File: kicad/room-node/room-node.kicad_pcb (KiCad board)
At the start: 4 copper layers, 90 x 50 mm, 59 parts, among them J1 USB4085-GF-A, J2 Speaker 8Ω, J3 Waveshare e-paper, J4 LED strip, SW1 TL3342 RESET, SW2 TL3342 BOOT, SW3 TL3342 VOICE, U1 ESP32-S3-WROOM-1-N16R8, U2 AP7361C-33ER-13, U3 MAX98357AETE+, U5 USBLC6-2SC6, U6 AHT20

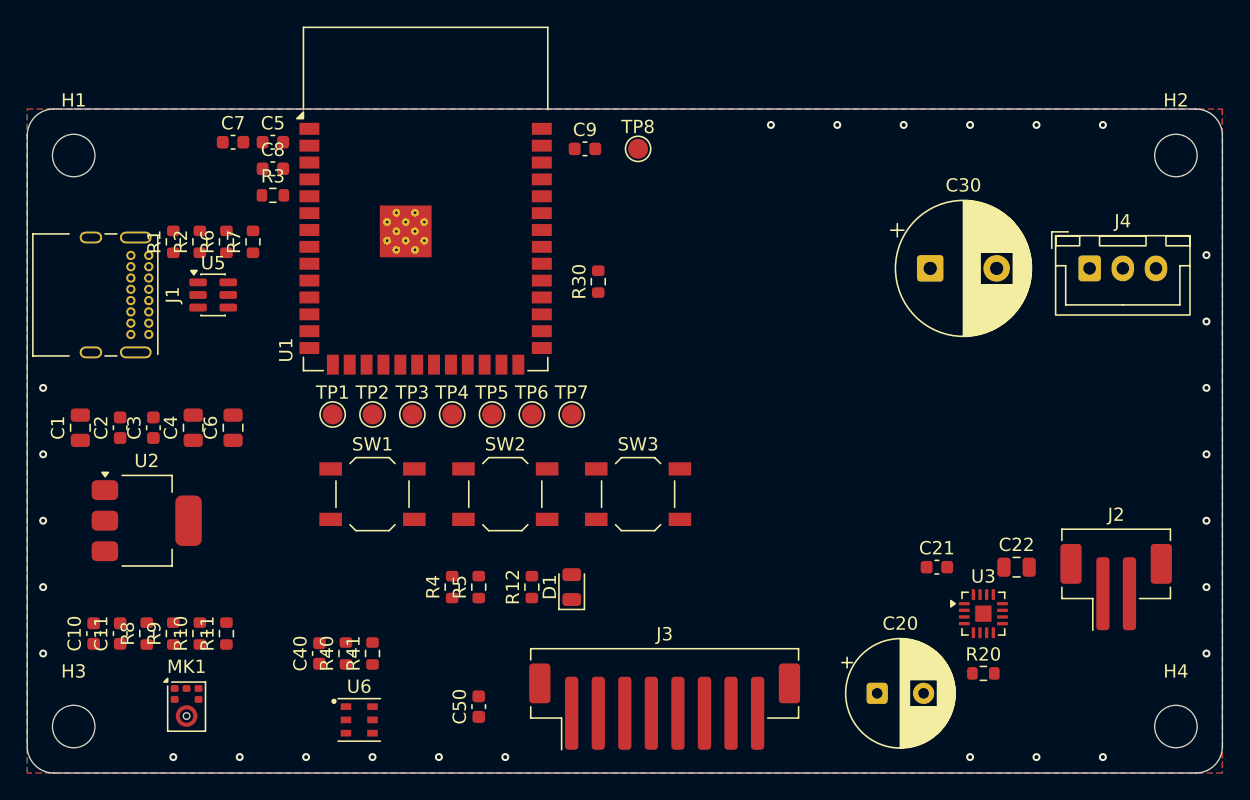
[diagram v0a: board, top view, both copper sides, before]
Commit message: SQU-17: full rev A board — display-size outline, placement and routing
Board matches the Waveshare 2.9" e-paper module (89.5 x 38 mm, 4 x M2 on its
84.5 x 33 mm hole pattern) so it screws behind the display on standoffs.
All 55 parts placed and every net routed (Freerouting + hand routes for J1 VBUS,
amp pins and the AHT20 island). L2 GND, L3 +3V3 planes; +5V as a 0.6-1.0 mm
track. DRC: 0 errors, 0 unconnected, 0 parity issues; 53 silkscreen warnings.

tools/pcb_build.py replaces tools/pcb_setup.py. Gerbers in reports/fab/.

Co-Authored-By: Claude Opus 5.5 <noreply@anthropic.com>
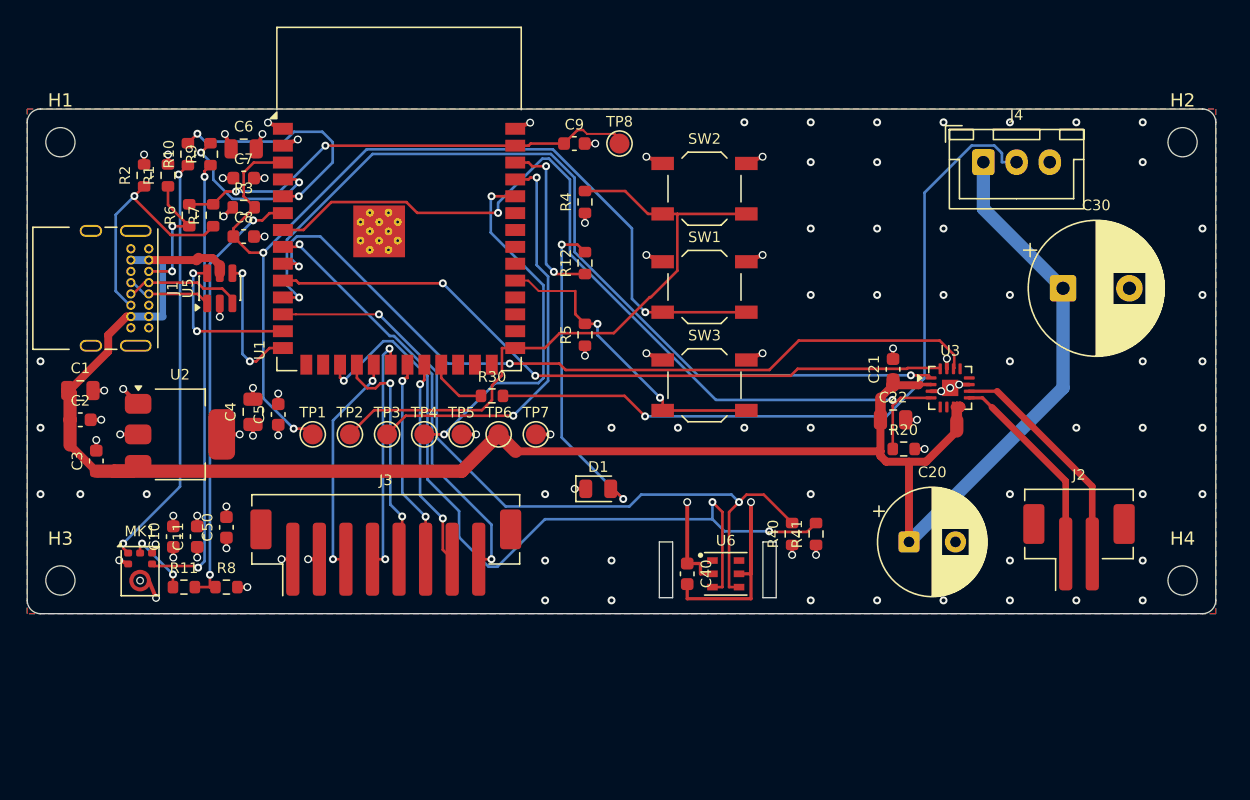
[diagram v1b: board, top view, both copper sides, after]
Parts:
- H1, H2, H3, H4: value M3 -> M2; footprint MountingHole:MountingHole_3.2mm_M3 -> MountingHole:MountingHole_2.2mm_M2
- moved R9 36.2 mm to (113.8, 103.4)
- moved R10 36.1 mm to (112.1, 103.4)
- moved R40 34.8 mm to (157.6, 132.0)
- moved R41 34.6 mm to (159.4, 132.0)
- moved R4 30.7 mm to (142.0, 107.0)
- moved U6 29.7 mm to (152.6, 135.0)
- moved SW1 29.5 mm to (151.0, 113.4)
- moved C40 28.3 mm to (149.7, 135.0), turned to -90 degrees
- moved SW2 27.5 mm to (151.0, 106.0)
- moved R12 24.7 mm to (142.0, 111.6)
- moved J3 24.0 mm to (127.0, 133.4)
- moved C50 23.3 mm to (115.0, 131.5)
- moved C6 21.0 mm to (116.3, 103.0), turned to 0 degrees
- moved R5 20.6 mm to (142.0, 117.0)
- moved C5 20.5 mm to (118.9, 123.0), turned to 90 degrees
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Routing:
- net +5V: track 0.00 -> 154.3 mm
- net EN: track 0.00 -> 75.4 mm, vias 0 -> 3
- net I2S_SPK_DIN: track 0.00 -> 67.4 mm, vias 0 -> 2
- net AMP_SD: track 0.00 -> 66.8 mm, vias 0 -> 2
- net I2C_SCL: track 0.00 -> 61.8 mm, vias 0 -> 3
- net I2S_SPK_LRCLK: track 0.00 -> 60.1 mm, vias 0 -> 2
- net Net-(J4-Pin_2): track 0.00 -> 56.9 mm, vias 0 -> 1
- net I2C_SDA: track 0.00 -> 56.4 mm, vias 0 -> 2
- net I2S_SPK_BCLK: track 0.00 -> 52.7 mm, vias 0 -> 2
- net GND: track 0.00 -> 49.7 mm, vias 27 -> 89
- net IO0: track 0.00 -> 48.8 mm
- net CC_SENSE: track 0.00 -> 35.3 mm, vias 0 -> 2
- net Net-(MK1-BCLK): track 0.00 -> 34.3 mm, vias 0 -> 2
- net I2S_MIC_DATA: track 0.00 -> 33.0 mm, vias 0 -> 2
- net EPD_BUSY: track 0.00 -> 32.2 mm, vias 0 -> 2
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- removed copper zone on In2.Cu, net +5V
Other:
- board size 90 x 50 mm -> 89.5 x 38 mm

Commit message: SQU-17: remove voice button SW3 + R5 (wake word only)
Chris: no voice button. U1 pin 31 (GPIO38) gets a no-connect flag.
Schematic, board (parts, 13 tracks/vias, +3V3 stub), BOM, docs,
pinout check and pcb_build.py updated. Gerbers, PDF, pictures regenerated.
ERC: 0 errors, 1 accepted warning. DRC: 0 errors, 0 unconnected,
0 parity issues, 53 silkscreen warnings. Pinout check: PASS.

Co-Authored-By: Claude Opus 5.5 <noreply@anthropic.com>
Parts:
- removed R5: 10k, Resistor_SMD:R_0603_1608Metric
- removed SW3: TL3342 VOICE, Button_Switch_SMD:SW_SPST_TL3342
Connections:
- U1 pad 31: VA_BTN -> unconnected-(U1-IO38-Pad31)
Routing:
- net VA_BTN: track 23.4 -> 0.00 mm, vias 2 -> 0
- net +3V3: track 23.9 -> 23.2 mm, vias 19 -> 18

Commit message: SQU-17: rev A board — apply design review fixes M1–M4 (SQU-31)
M1 C21 (0.1 uF) and C22 (10 uF) moved from U3 pin 2 (GAIN_SLOT) to the VDD
   pins 7/8: C21 0.7 mm below the pins, C22 under it, each GND pad with its
   own via to L2.
M2 +5V LED/amp path: no 0.6 mm sections left. J1 -> C1 doubled on F.Cu and
   B.Cu through the USB-C pin row, 1.2 mm round C1; C2 -> C3 1.2 mm; new
   1.5 mm run from TP6 to C20 (replaces the 0.6 mm run along y = 125.8);
   1.0 mm to the amp pins.
M3 U2 tab on a F.Cu +3V3 copper area (full connection) with 5 vias to the
   L3 plane (the tab had none: fan-out tested the tab width, not its height;
   fixed in pcb_build.py).
M4 AMP_SD under U1 moved to y = 106.4, 0.76 mm from the module GND pad
   (was 0.15 mm).

DRC: 0 errors, 0 unconnected, 0 parity issues, 51 silkscreen warnings.
Gerbers, DRC report, pictures and layout.md updated.

Co-Authored-By: Claude Opus 5.5 <noreply@anthropic.com>
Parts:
- moved C21 7.10 mm to (170.8, 124.0), turned to 0 degrees
- moved C22 6.26 mm to (171.0, 125.8)
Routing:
- net +5V: track 154.3 -> 170.3 mm, vias 0 -> 2
- net AMP_SD: track 66.8 -> 67.3 mm
- net GND: track 49.7 -> 50.0 mm, vias 89 -> 91
- net +3V3: vias 18 -> 22
- added copper zone on F.Cu, net +3V3

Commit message: SQU-32: J3 side entry (S8B-PH-SM4-TB) + SQU-31 review polish
J3 swapped from the top-entry B8B-PH-SM4-TB to the side-entry
S8B-PH-SM4-TB, mouth facing out over the bottom board edge so the cable
reaches the display behind the board. Same pinout, pin 1 to pin 1.
Housing front face 0.52 mm inside the edge, limited by the mounting-tab
pads (0.32 mm copper to edge). Each pin gets a via at y = 133.90 behind
the pad row with a 2.4 mm F.Cu stub forward into the pad; the six EPD
B.Cu drops were re-aimed at that row.

Review polish from SQU-31:
- C6 rotated 180 deg, 2.01 mm 0.3 mm F.Cu track to U1 pin 2
- CC_SENSE cross-module run 102.76 -> 105.90 (2.76 -> 5.90 mm below the
  antenna line)
- mic hole: GND via moved to 2.61 mm from the hole (was 1.77 mm)
- AHT20 island neck slot 1.00 x 1.25 mm, neck 6.80 -> 5.80 mm
- U3 pin 11 GND via moved 1.49 mm clear of the exposed pad
- U2 tab via column x 116.0 -> 116.3
- +5V bottom row 1.0/1.2 -> 1.5 mm (1.4 mm past the U2 tab),
  C1->C2->C3 1.0 -> 1.2 mm
- U3 pins 7/8 feed necked to the 0.25 mm pad width for the last 0.70 mm
- 23 reference designators moved off pads, silk and the board edge
- layout.md: U2 via wording, J3, DRC counts

Skipped, with the numbers in the issue: the C40 -> U6 pin 5 direct GND
track and the U3 pin 3 via, neither of which fits.

ERC 0 errors (1 pre-existing warning), DRC 0 errors / 0 unconnected /
0 parity, 51 -> 5 silk warnings, tools/check_pinout.py PASS.
Gerbers, schematic PDF and renders in reports/ regenerated.

Co-Authored-By: Paperclip <noreply@paperclip.ing>
Co-Authored-By: Claude Opus 5 <noreply@anthropic.com>
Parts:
- J3: footprint Connector_JST:JST_PH_B8B-PH-SM4-TB_1x08-1MP_P2.00mm_Vertical -> Connector_JST:JST_PH_S8B-PH-SM4-TB_1x08-1MP_P2.00mm_Horizontal
- moved J3 1.05 mm to (128.0, 133.1)
- turned C6 to 180 degrees
- turned C7 to 180 degrees
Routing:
- net CC_SENSE: track 35.3 -> 41.6 mm
- net EPD_RST: track 15.8 -> 18.6 mm
- net EPD_DC: track 15.6 -> 18.4 mm
- net +3V3: track 23.2 -> 25.8 mm, vias 22 -> 21
- net EPD_CS: track 17.7 -> 20.3 mm
- net GND: track 50.0 -> 52.5 mm
- net EPD_CLK: track 18.3 -> 19.8 mm
- net EPD_BUSY: track 32.2 -> 33.6 mm
- net EPD_MOSI: track 16.9 -> 17.5 mm
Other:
- outline, holes or cut-outs redrawn

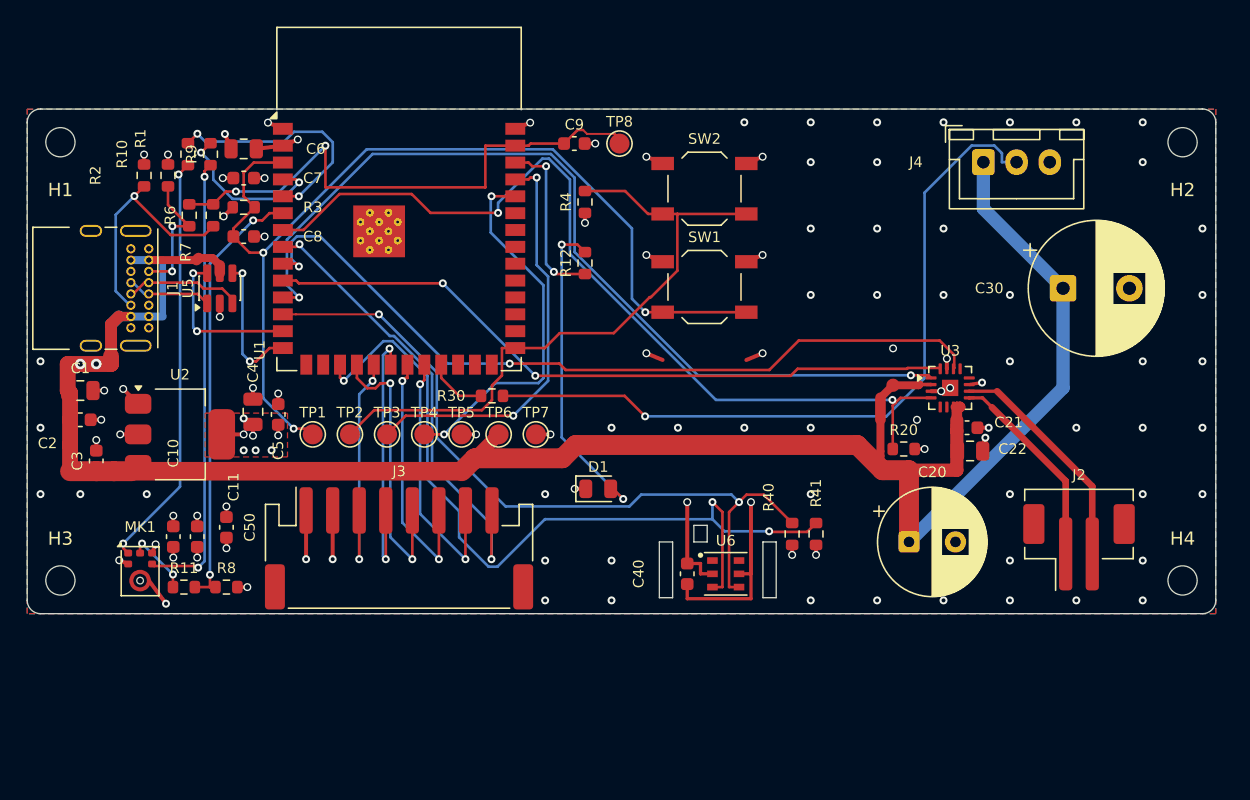
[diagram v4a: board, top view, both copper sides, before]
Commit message: SQU-35: rev A connectors to the board edges (J3 right, J1 + J4 left)
Chris's ask: short cables when the board sits behind the display. Each
connector now leaves the edge nearest what it plugs into. Frame of
reference as in docs/pcb/layout.md: parts side, USB-C on the left.

- J1 USB-C unchanged on the left edge, (109.155, 110.525).
- J4 LED strip -> (103.500, 122.300), left edge directly below J1.
  J1 VBUS pad B4 -> J4 pin 1 is 7.94 mm (was 65.24 mm).
- C30 1000 uF -> (114.500, 125.800), the next part along the trunk,
  0.21 mm from J4's courtyard. J1 -> C30 pad 1 is 12.18 mm (was 70.23).
- J3 display -> (184.600, 117.500) rot 90, right edge, side-entry mouth
  over the edge. Mounting-tab copper at x = 189.20, exactly the 0.30 mm
  copper-to-edge limit. Pin 1 is the lower pad, (181.75, 124.50), marked
  with a filled silk triangle tipped at (179.70, 124.50).
- Mic sound hole stays at (108.50, 135.51): J4 did not move it, nearest
  point of its courtyard is 9.26 mm away. A new 2.5 mm "MK1 gasket seat"
  via keep-out guarantees nothing lands inside 2.0 mm of the hole.

Re-placed around them: U2 + C3/C4/C5 moved as one rigid block by
(+58.5, -19.9) into the top-right spot the LED connector left, so the
reviewed M3 tab copper and its 5 vias are geometrically unchanged; the
LDO tab is 37.26 mm from the AHT20 (was 38.41 mm). J2 -> (176.300,
133.000) and C20 -> (165.000, 132.600) to clear J3; C22 -> y 126.0 for a
0.20 mm courtyard gap; C50 follows J3 to (177.500, 121.000); C1/C2, the
mic passives and the TP1-TP7 row shifted out of the new trunk's way.

The +5V net is now hand routed end to end instead of left to the router:
1.50 mm B.Cu from J1 to J4/C30 (21.3 mm) and along the bottom spine to
C20 (59.3 mm), 1.00 mm branches to TP6, C1/C2 and the LDO, 0.80/0.25 mm
only at U3's 0.5 mm-pitch pins. Nothing on the LED path is below 1.5 mm.

Two review findings are now rules in the generator rather than one-shot
patches, so a rebuild cannot lose them: an antenna-end rule area
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
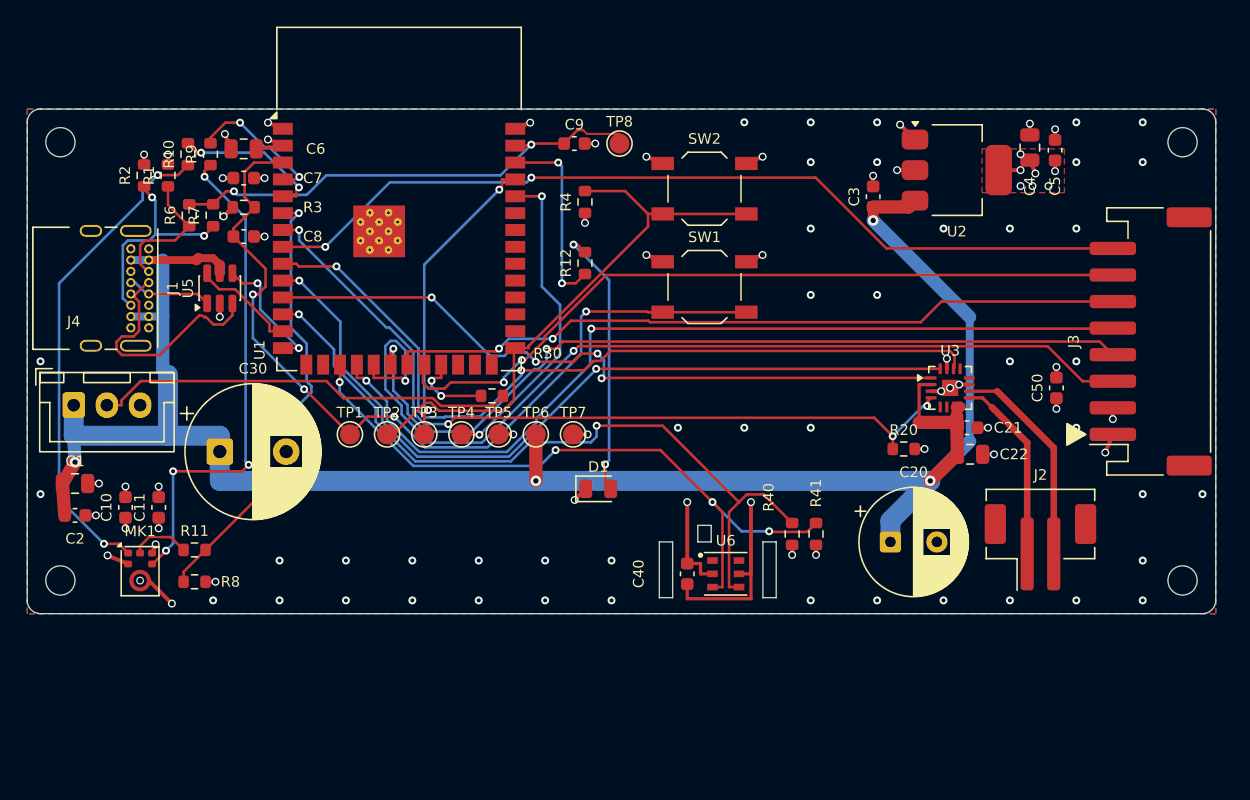
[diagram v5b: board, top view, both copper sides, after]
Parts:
- moved J4 70.9 mm to (103.5, 122.3)
- moved C30 64.7 mm to (114.5, 125.8)
- moved C50 63.4 mm to (177.5, 121.0)
- moved C5 61.8 mm to (177.4, 103.1)
- moved U2 61.8 mm to (170.0, 104.6)
- moved C3 61.8 mm to (163.7, 106.6)
- moved C4 61.8 mm to (175.5, 102.9)
- moved J3 58.7 mm to (184.6, 117.5), turned to 90 degrees
- moved C2 7.21 mm to (103.6, 130.6)
- moved C1 7.01 mm to (103.6, 128.2)
- moved C10 4.22 mm to (107.4, 130.0)
- moved C11 3.64 mm to (109.9, 130.0)
- moved R11 2.91 mm to (112.6, 133.2)
- moved J2 2.90 mm to (176.3, 133.0)
- moved TP3 2.80 mm to (129.9, 124.5)
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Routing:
- net EPD_MOSI: track 17.5 -> 71.9 mm
- net EPD_CS: track 20.3 -> 66.6 mm
- net EPD_CLK: track 19.8 -> 64.1 mm
- net EPD_RST: track 18.6 -> 57.5 mm
- net EPD_DC: track 18.4 -> 55.8 mm
- net EPD_BUSY: track 33.6 -> 66.9 mm
- net Net-(J4-Pin_2): track 56.9 -> 31.9 mm, vias 1 -> 0
- net +5V: track 170.7 -> 152.9 mm, vias 2 -> 4
- net I2S_SPK_DIN: track 67.4 -> 53.1 mm, vias 2 -> 4
- net I2C_SCL: track 61.8 -> 51.0 mm, vias 3 -> 4
- net USB_D+_CONN: track 8.85 -> 18.9 mm
- net EN: track 75.4 -> 65.8 mm, vias 3 -> 4
- net TXD0: track 31.1 -> 22.9 mm
- net I2S_SPK_BCLK: track 52.7 -> 60.3 mm
- net I2S_MIC_WS: track 18.4 -> 11.5 mm
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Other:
- outline, holes or cut-outs redrawn
